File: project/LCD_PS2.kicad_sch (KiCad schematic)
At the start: 8 parts, among them T1 BC546, X3 TIMER, X4 KEYBOARD

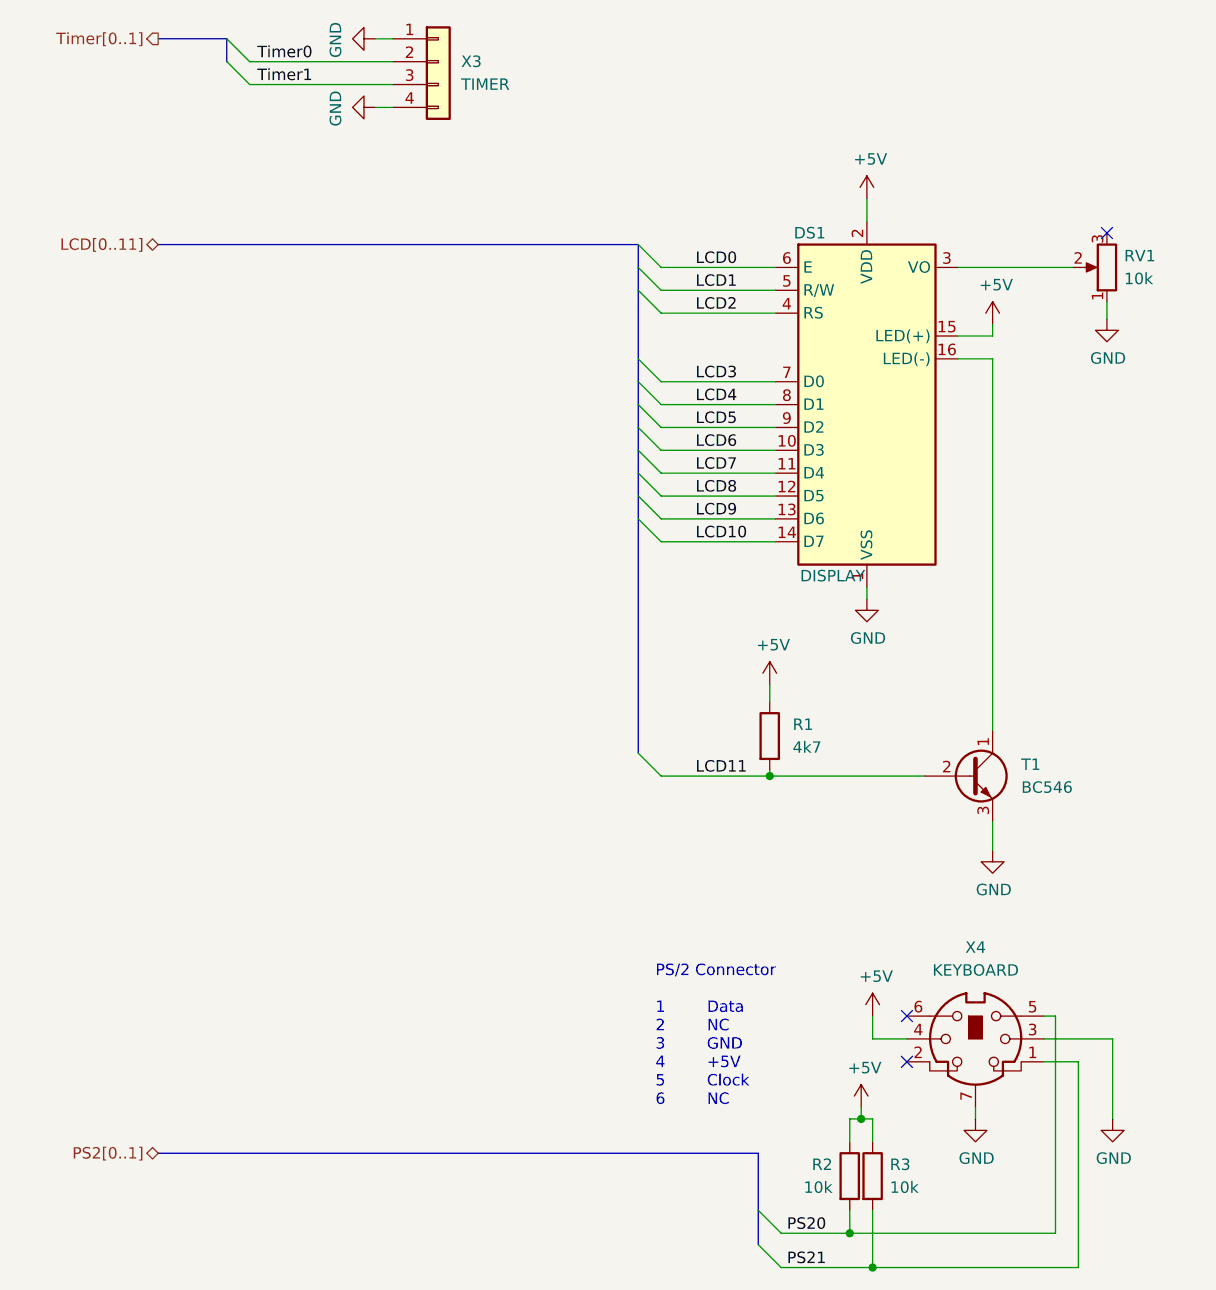
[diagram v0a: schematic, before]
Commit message: Fix grid issues, fix missing libraries, replace FT232 with FT231
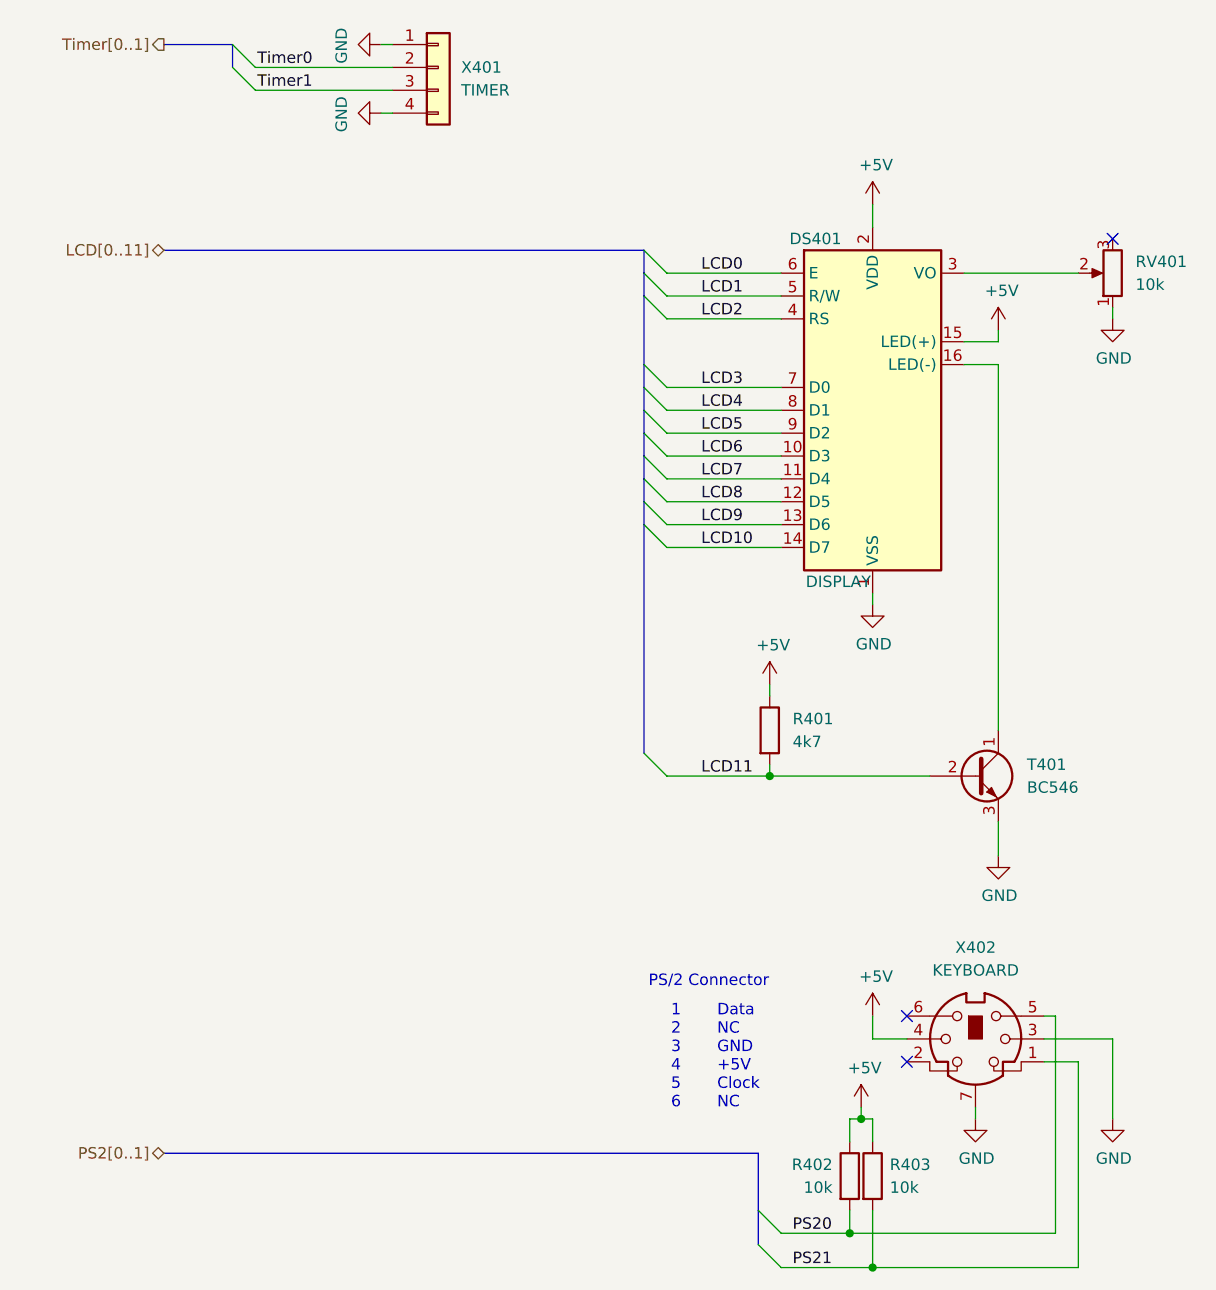
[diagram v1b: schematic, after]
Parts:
- RV401: renamed from RV1; symbol Device:R_POT -> Device:R_Potentiometer
- X402: renamed from X4; Mfr. TE Connectivity / AMP -> TE Connectivity; Mfr. No. 5749231-1 -> 5749180-1; Mouser 571-5749231-1 -> 571-5749180-1
- renumbered DS1 to DS401, R1 to R401, R2 to R402, R3 to R403, T1 to T401, X3 to X401
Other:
- note added: "1 2 3 4 5 6"
- note added: "PS/2 Connector"
- note removed: "PS/2 Connector 1 2 3 4 5 6"
- moved on the sheet: DS401, R401, RV401, T401, X401

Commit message: Fix swapped DM and DP, add missing datasheets, remove Mouser property
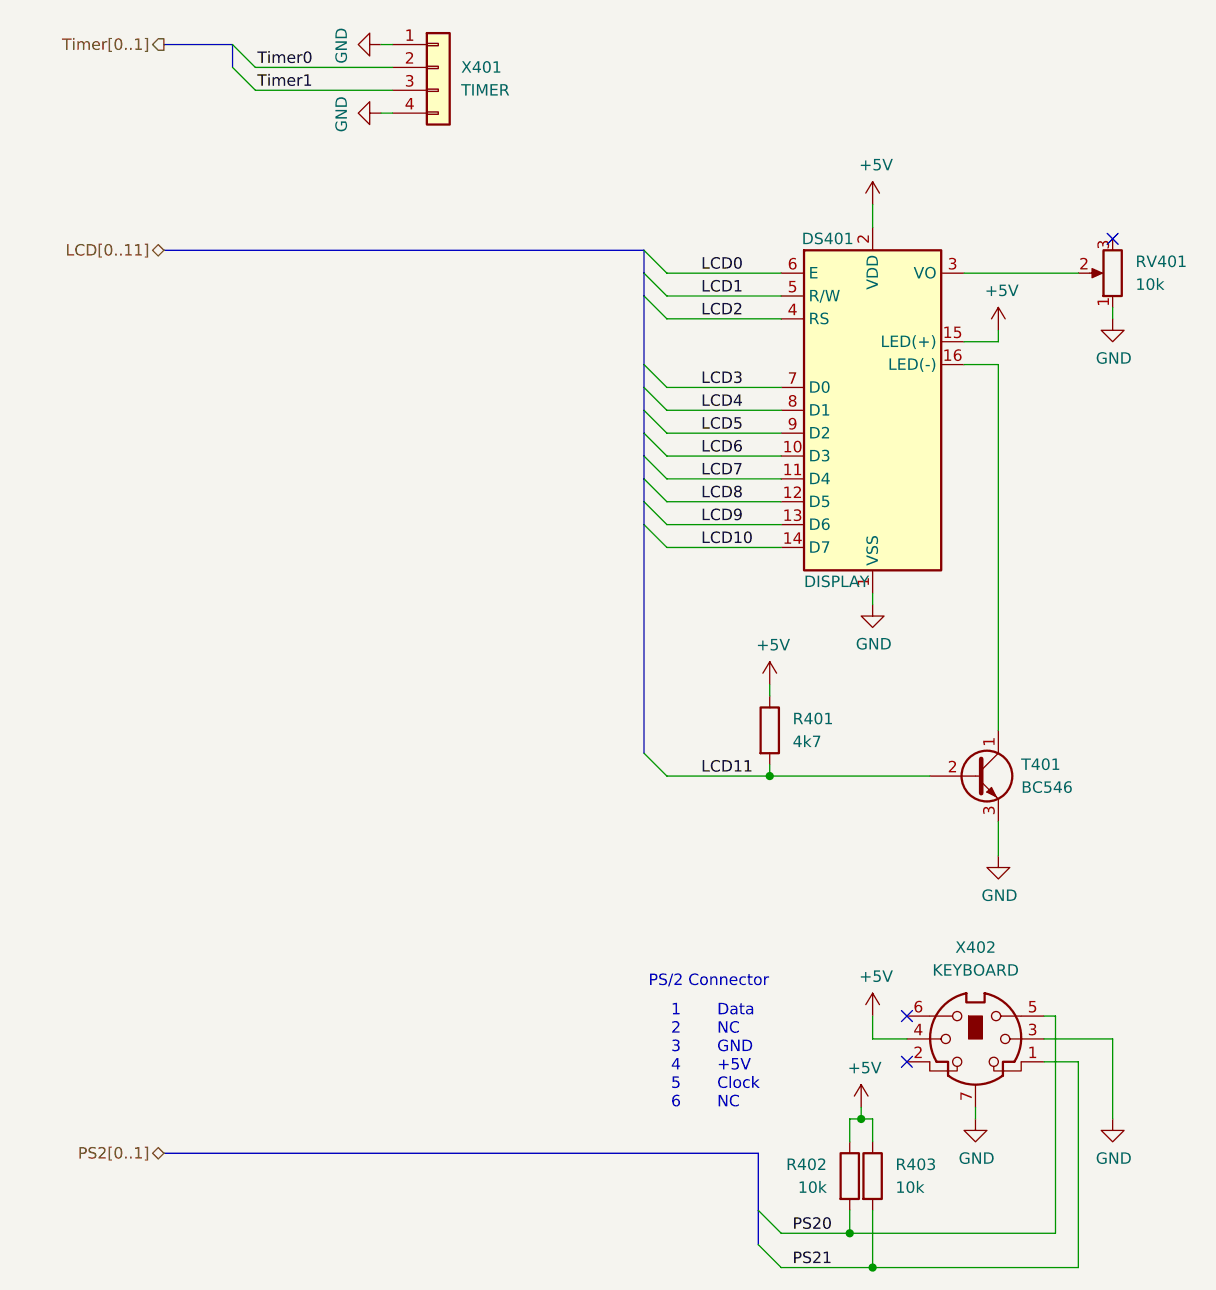
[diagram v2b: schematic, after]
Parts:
- DS401: Mouser 763-0220GZ-FSW-GBW -> (none)
- R401: Mouser 603-MFP-25BRD52-4K7 -> (none)
- R402, R403: Mouser 603-MFP-25BRD52-10K -> (none)
- RV401: Mouser 652-3386Y-1-103LF -> (none)
- T401: Mouser 512-BC546CTA -> (none)
- X401: Mouser 571-826926-4 -> (none)
- X402: Mouser 571-5749180-1 -> (none)
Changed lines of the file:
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@@
 		(dnp no)
 		(property "Reference" "DS401"
-			(at 123.19 52.07 0)
-			(effects
-				(font
-					(size 1.27 1.27)
-				)
+			(at 121.666 52.07 0)
+			(effects
+				(font
+					(size 1.27 1.27)
+				)
+				(justify left)
 			)
 		)
 		(property "Value" "DISPLAY"
-			(at 125.73 90.17 0)
-			(effects
-				(font
-					(size 1.27 1.27)
-				)
+			(at 121.92 90.17 0)
+			(effects
+				(font
+					(size 1.27 1.27)
+				)
+				(justify left)
 			)
 		)
@@
 		)
 		(property "Mfr. No." "NHD-0220GZ-FSW-GBW-L"
-			(at 129.54 71.12 0)
-			(effects
-				(font
-					(size 1.27 1.27)
-				)
-				(hide yes)
-			)
-		)
-		(property "Mouser" "763-0220GZ-FSW-GBW"
 			(at 129.54 71.12 0)
 			(effects
@@
 			)
 		)
-		(property "Mouser" "571-5749180-1"
-			(at 140.97 140.97 0)
-			(effects
-				(font
-					(size 1.27 1.27)
-				)
-				(hide yes)
-			)
-		)
 		(property "Distributor" "Mouser"
 			(at 140.97 140.97 0)
@@
 			)
 		)
-		(property "Datasheet" "~"
+		(property "Datasheet" "https://www.mouser.de/datasheet/2/54/3386-776606.pdf"
 			(at 156.21 55.88 0)
 			(effects
@@
 			)
 		)
-		(property "Mouser" "652-3386Y-1-103LF"
-			(at 156.21 55.88 0)
-			(effects
-				(font
-					(size 1.27 1.27)
-				)
-				(hide yes)
-			)
-		)
 		(property "Distributor" "Mouser"
 			(at 156.21 55.88 0)
@@
 		(fields_autoplaced yes)
 		(property "Reference" "R402"
-			(at 125.095 154.9399 0)
+			(at 124.46 154.9399 0)
 			(effects
 				(font
@@
 		)
 		(property "Value" "10k"
-			(at 125.095 157.4799 0)
+			(at 124.46 157.4799 0)
 			(effects
 				(font
@@
 			)
 		)
-		(property "Datasheet" "~"
+		(property "Datasheet" "https://www.mouser.de/datasheet/2/447/YAGEO_MFP_datasheet_2024v3-3447153.pdf"
 			(at 127 156.21 0)
 			(effects
@@
 			)
 		)
-		(property "Mouser" "603-MFP-25BRD52-10K"
-			(at 127 156.21 0)
-			(effects
-				(font
-					(size 1.27 1.27)
-				)
-				(hide yes)
-			)
-		)
 		(property "Distributor" "Mouser"
 			(at 127 156.21 0)
@@
 		(fields_autoplaced yes)
 		(property "Reference" "R403"
-			(at 131.445 154.9399 0)
+			(at 132.08 154.9399 0)
 			(effects
 				(font
@@
 		)
 		(property "Value" "10k"
-			(at 131.445 157.4799 0)
+			(at 132.08 157.4799 0)
 			(effects
 				(font
@@
 			)
 		)
-		(property "Datasheet" "~"
+		(property "Datasheet" "https://www.mouser.de/datasheet/2/447/YAGEO_MFP_datasheet_2024v3-3447153.pdf"
 			(at 129.54 156.21 0)
 			(effects
@@
 			)
 		)
-		(property "Mouser" "603-MFP-25BRD52-10K"
-			(at 129.54 156.21 0)
-			(effects
-				(font
-					(size 1.27 1.27)
-				)
-				(hide yes)
-			)
-		)
 		(property "Distributor" "Mouser"
 			(at 129.54 156.21 0)
@@
 		(fields_autoplaced yes)
 		(property "Reference" "T401"
-			(at 146.685 110.4899 0)
+			(at 146.05 110.4899 0)
 			(effects
 				(font
@@
 		)
 		(property "Value" "BC546"
-			(at 146.685 113.0299 0)
+			(at 146.05 113.0299 0)
 			(effects
 				(font
@@
 		)
 		(property "Mfr. No." "BC546CTA"
-			(at 140.97 111.76 0)
-			(effects
-				(font
-					(size 1.27 1.27)
-				)
-				(hide yes)
-			)
-		)
-		(property "Mouser" "512-BC546CTA"
 			(at 140.97 111.76 0)
 			(effects
@@
 			)
 		)
-		(property "Mouser" "603-MFP-25BRD52-4K7"
-			(at 118.11 106.68 0)
-			(effects
-				(font
-					(size 1.27 1.27)
-				)
-				(hide yes)
-			)
-		)
 		(property "Distributor" "Mouser"
 			(at 118.11 106.68 0)
@@
 			)
 		)
-		(property "Datasheet" "~"
+		(property "Datasheet" "https://www.mouser.de/datasheet/2/418/7/ENG_CD_826629_AC1-2068659.pdf"
 			(at 81.28 33.02 0)
 			(effects
@@
 			(at 81.28 33.02 0)
 			(effects
-				(font
-					(size 1.27 1.27)
-				)
-				(hide yes)
-			)
-		)
-		(property "Mouser" "571-826926-4"
-			(at 81.28 33.02 0)
-			(effects
